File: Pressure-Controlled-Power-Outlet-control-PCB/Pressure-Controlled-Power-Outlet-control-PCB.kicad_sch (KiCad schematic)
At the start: 25 parts, among them J1 Analog water pressure sensor 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, J2 1017514, K1 PR27-24V-S-900-1A-EF, K2 PR27-24V-S-900-1A-EF, Q1 2N3906, Q2 IRF540N, Q3 IRF540N, Q4 2N3906, U1 Pico, U2 LM324, U3 LF50_TO220

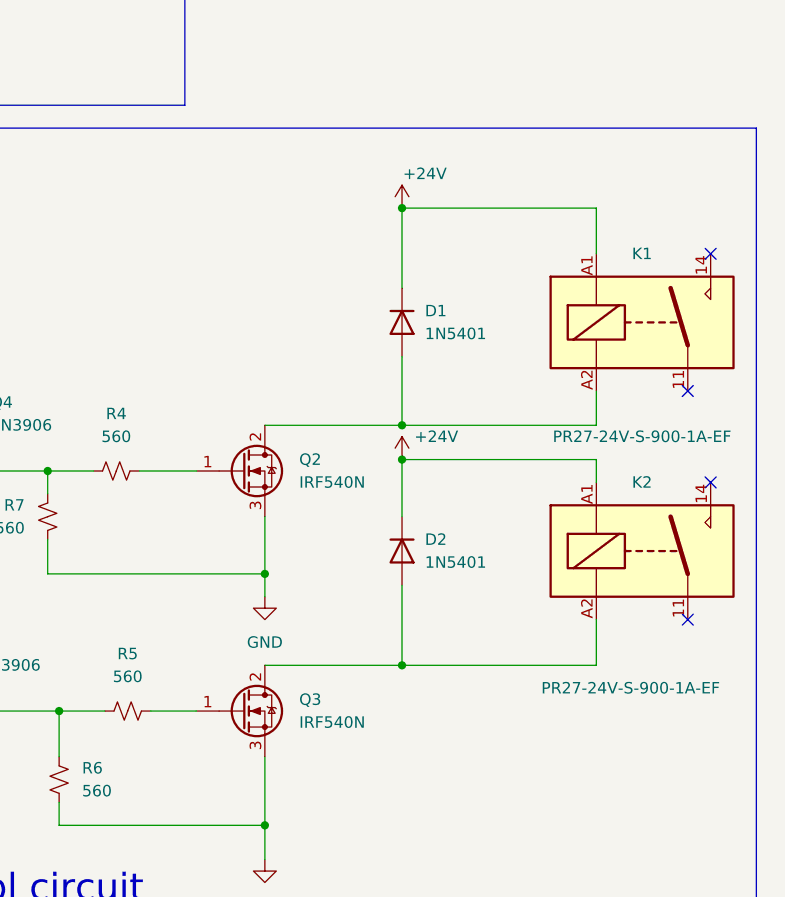
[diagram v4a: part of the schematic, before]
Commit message: added new relays
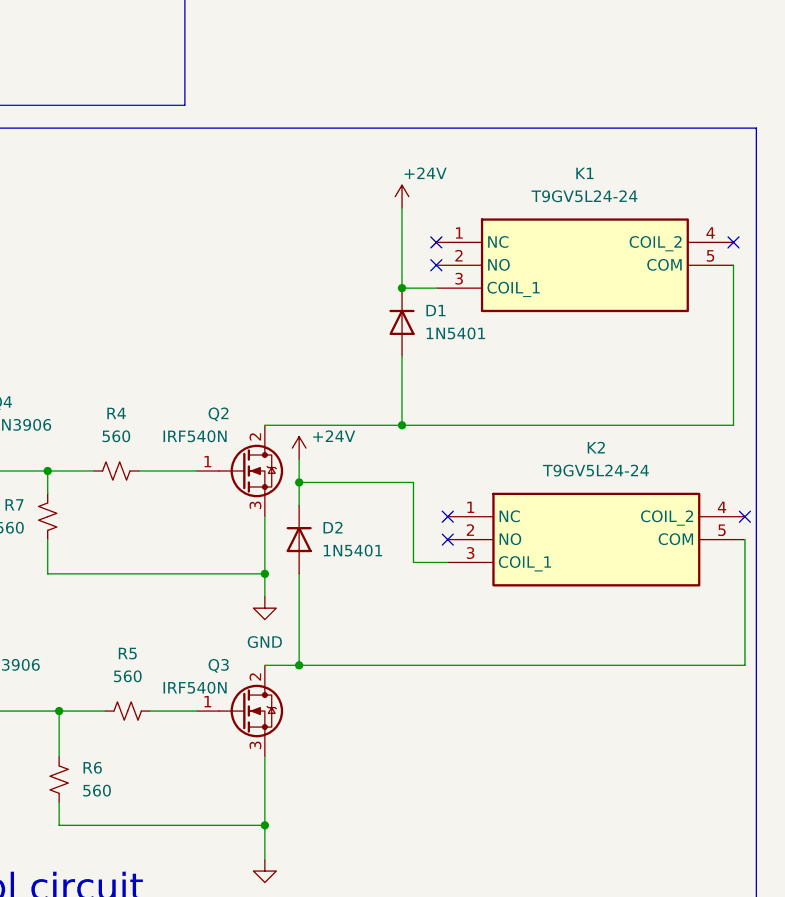
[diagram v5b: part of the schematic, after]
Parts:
- removed K1, K2: PR27-24V-S-900-1A-EF, Relay_THT:Relay_1-Form-A_Schrack-RYII_RM5mm, symbol Relay:Relay_SPST-NO
- added K1, K2: T9GV5L24-24, Extra:T9GV5L2424, symbol Extra:T9GV5L24-24
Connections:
- net +24V: now also K1.3 (COIL_1), K2.3 (COIL_1)
- net at D2.2 (A), Q3.2 (D): now also K2.5 (COM)
- net at D1.2 (A), Q2.2 (D): now also K1.5 (COM)
- no-connect marks 33 -> 35
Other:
- moved on the sheet: D2

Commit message: fixed PCB
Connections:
- net at D2.2 (A), Q3.2 (D): now also K2.4 (COIL_2); no longer K2.5 (COM)
- net at D1.2 (A), Q2.2 (D): now also K1.4 (COIL_2); no longer K1.5 (COM)
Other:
- moved on the sheet: K2
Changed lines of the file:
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@@
   )
   (no_connect (at 68.58 101.6))
-  (no_connect (at 245.11 106.68))
+  (no_connect (at 242.57 106.68))
   (no_connect (at 53.34 134.62))
   (no_connect (at 48.26 134.62))
@@
   (no_connect (at 68.58 83.82))
   (no_connect (at 33.02 104.14))
+  (no_connect (at 275.59 106.68))
   (no_connect (at 68.58 109.22))
-  (no_connect (at 278.13 104.14))
   (no_connect (at 33.02 88.9))
   (no_connect (at 33.02 116.84))
@@
   (no_connect (at 33.02 129.54))
   (no_connect (at 33.02 106.68))
+  (no_connect (at 276.86 76.2))
   (no_connect (at 68.58 91.44))
   (no_connect (at 33.02 127))
-  (no_connect (at 276.86 73.66))
   (no_connect (at 33.02 121.92))
   (no_connect (at 68.58 119.38))
   (no_connect (at 68.58 116.84))
   (no_connect (at 68.58 106.68))
-  (no_connect (at 245.11 104.14))
+  (no_connect (at 242.57 104.14))
   (no_connect (at 68.58 121.92))
   (no_connect (at 68.58 96.52))
@@
     (stroke (width 0) (type default))
   )
+  (wire (pts (xy 278.13 73.66) (xy 276.86 73.66))
+    (stroke (width 0) (type default))
+  )
   (wire (pts (xy 191.77 99.06) (xy 200.66 99.06))
     (stroke (width 0) (type default))
   )
-  (wire (pts (xy 278.13 106.68) (xy 278.13 120.65))
-    (stroke (width 0) (type default))
-  )
   (wire (pts (xy 162.56 40.64) (xy 162.56 43.18))
     (stroke (width 0) (type default))
   )
-  (wire (pts (xy 245.11 109.22) (xy 241.3 109.22))
+  (wire (pts (xy 242.57 109.22) (xy 241.3 109.22))
     (stroke (width 0) (type default))
   )
@@
     (stroke (width 0) (type default))
   )
+  (wire (pts (xy 278.13 120.65) (xy 278.13 104.14))
+    (stroke (width 0) (type default))
+  )
   (wire (pts (xy 241.3 109.22) (xy 241.3 100.33))
     (stroke (width 0) (type default))
@@
     (stroke (width 0) (type default))
   )
-  (wire (pts (xy 278.13 120.65) (xy 228.6 120.65))
+  (wire (pts (xy 228.6 120.65) (xy 278.13 120.65))
     (stroke (width 0) (type default))
   )
@@
     (stroke (width 0) (type default))
   )
+  (wire (pts (xy 240.03 93.98) (xy 278.13 93.98))
+    (stroke (width 0) (type default))
+  )
   (wire (pts (xy 175.26 119.38) (xy 182.88 119.38))
     (stroke (width 0) (type default))
@@
     (stroke (width 0) (type default))
   )
+  (wire (pts (xy 278.13 104.14) (xy 275.59 104.14))
+    (stroke (width 0) (type default))
+  )
   (wire (pts (xy 210.82 99.06) (xy 217.17 99.06))
     (stroke (width 0) (type default))
   )
+  (wire (pts (xy 278.13 93.98) (xy 278.13 73.66))
+    (stroke (width 0) (type default))
+  )
   (wire (pts (xy 212.09 125.73) (xy 217.17 125.73))
     (stroke (width 0) (type default))
@@
     (stroke (width 0) (type default))
   )
-  (wire (pts (xy 276.86 76.2) (xy 276.86 93.98))
-    (stroke (width 0) (type default))
-  )
   (wire (pts (xy 76.2 115.57) (xy 76.2 111.76))
     (stroke (width 0) (type default))
@@
   )
   (wire (pts (xy 114.3 168.91) (xy 111.76 168.91))
-    (stroke (width 0) (type default))
-  )
-  (wire (pts (xy 276.86 93.98) (xy 240.03 93.98))
     (stroke (width 0) (type default))
   )
@@
     )
   )
-  (symbol (lib_id "Extra:T9GV5L24-24") (at 245.11 104.14 0) (unit 1)
-    (in_bom yes) (on_board yes) (dnp no) (fields_autoplaced)
-    (property "Reference" "K2" (at 261.62 96.52 0)
-      (effects (font (size 1.27 1.27)))
-    )
-    (property "Value" "T9GV5L24-24" (at 261.62 99.06 0)
-      (effects (font (size 1.27 1.27)))
-    )
-    (property "Footprint" "Extra:T9GV5L2424" (at 274.32 199.06 0)
-      (effects (font (size 1.27 1.27)) (justify left top) hide)
-    )
-    (property "Datasheet" "https://www.te.com/commerce/DocumentDelivery/DDEController?Action=srchrtrv&DocNm=T9G&DocType=Data%20Sheet&DocLang=English&PartCntxt=1558670-7&DocFormat=pdf" (at 274.32 299.06 0)
-      (effects (font (size 1.27 1.27)) (justify left top) hide)
-    )
-    (property "Height" "27" (at 274.32 499.06 0)
-      (effects (font (size 1.27 1.27)) (justify left top) hide)
-    )
-    (property "Mouser Part Number" "655-T9GV5L24-24" (at 274.32 599.06 0)
-      (effects (font (size 1.27 1.27)) (justify left top) hide)
-    )
-    (property "Mouser Price/Stock" "https://www.mouser.co.uk/ProductDetail/TE-Connectivity-PB/T9GV5L24-24?qs=f9yNj16SXrJ%2FH2bWvrJZwA%3D%3D" (at 274.32 699.06 0)
-      (effects (font (size 1.27 1.27)) (justify left top) hide)
-    )
-    (property "Manufacturer_Name" "TE Connectivity" (at 274.32 799.06 0)
-      (effects (font (size 1.27 1.27)) (justify left top) hide)
-    )
-    (property "Manufacturer_Part_Number" "T9GV5L24-24" (at 274.32 899.06 0)
-      (effects (font (size 1.27 1.27)) (justify left top) hide)
-    )
+  (symbol (lib_id "Extra:T9GV5L24-24") (at 242.57 104.14 0) (unit 1)
+    (in_bom yes) (on_board yes) (dnp no) (fields_autoplaced)
+    (property "Reference" "K2" (at 259.08 96.52 0)
+      (effects (font (size 1.27 1.27)))
+    )
+    (property "Value" "T9GV5L24-24" (at 259.08 99.06 0)
+      (effects (font (size 1.27 1.27)))
+    )
+    (property "Footprint" "Extra:T9GV5L2424" (at 271.78 199.06 0)
+      (effects (font (size 1.27 1.27)) (justify left top) hide)
+    )
+    (property "Datasheet" "https://www.te.com/commerce/DocumentDelivery/DDEController?Action=srchrtrv&DocNm=T9G&DocType=Data%20Sheet&DocLang=English&PartCntxt=1558670-7&DocFormat=pdf" (at 271.78 299.06 0)
+      (effects (font (size 1.27 1.27)) (justify left top) hide)
+    )
+    (property "Height" "27" (at 271.78 499.06 0)
+      (effects (font (size 1.27 1.27)) (justify left top) hide)
+    )
+    (property "Mouser Part Number" "655-T9GV5L24-24" (at 271.78 599.06 0)
+      (effects (font (size 1.27 1.27)) (justify left top) hide)
+    )
+    (property "Mouser Price/Stock" "https://www.mouser.co.uk/ProductDetail/TE-Connectivity-PB/T9GV5L24-24?qs=f9yNj16SXrJ%2FH2bWvrJZwA%3D%3D" (at 271.78 699.06 0)
+      (effects (font (size 1.27 1.27)) (justify left top) hide)
+    )
+    (property "Manufacturer_Name" "TE Connectivity" (at 271.78 799.06 0)
+      (effects (font (size 1.27 1.27)) (justify left top) hide)
+    )
+    (property "Manufacturer_Part_Number" "T9GV5L24-24" (at 271.78 899.06 0)
+      (effects (font (size 1.27 1.27)) (justify left top) hide)
+    )

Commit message: should be done need to review the board to ensure everything is good
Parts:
- added unit 5 of U2
- R4, R5, R6, R7: value 560 -> 560 Ohm
- R8, R9: value 10K -> 10KOhm
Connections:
- net +5V: now also U2.4 (V+)
- net GND: now also U2.11 (V-)
- net ADC_Ref: no longer names the net of U1.35 (ADC_VREF)
- no-connect marks 35 -> 36
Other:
- title: (none) -> Pressure Controlled Power Outlet
- moved on the sheet: R3
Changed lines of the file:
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@@
 (kicad_sch (version 20230121) (generator eeschema)
   (paper "A4")
+  (title_block
+    (title "Pressure Controlled Power Outlet")
+    (date "2024-07-18")
+    (rev "V1.0")
+  )
   (junction (at 121.92 175.26) (diameter 0) (color 0 0 0 0)
   )
@@
   (no_connect (at 275.59 106.68))
   (no_connect (at 68.58 109.22))
+  (no_connect (at 68.58 93.98))
   (no_connect (at 33.02 88.9))
   (no_connect (at 33.02 116.84))
@@
     (stroke (width 0) (type default))
   )
-  (wire (pts (xy 77.47 99.06) (xy 91.44 99.06))
+  (wire (pts (xy 80.01 99.06) (xy 91.44 99.06))
     (stroke (width 0) (type default))
   )
@@
     (stroke (width 0) (type default))
   )
-  (wire (pts (xy 76.2 93.98) (xy 68.58 93.98))
-    (stroke (width 0) (type default))
-  )
   (wire (pts (xy 228.6 120.65) (xy 278.13 120.65))
     (stroke (width 0) (type default))
@@
     (stroke (width 0) (type default))
   )
-  (wire (pts (xy 68.58 99.06) (xy 72.39 99.06))
+  (wire (pts (xy 68.58 99.06) (xy 74.93 99.06))
     (stroke (width 0) (type default))
   )
@@
     (effects (font (size 1.27 1.27)) (justify right bottom))
   )
-  (label "ADC_Ref" (at 76.2 93.98 0) (fields_autoplaced)
-    (effects (font (size 1.27 1.27)) (justify left bottom))
-  )
   (label "Activate_Neutral" (at 166.37 119.38 180) (fields_autoplaced)
     (effects (font (size 1.27 1.27)) (justify right bottom))
@@
       (effects (font (size 1.27 1.27)))
     )
-    (property "Value" "10K" (at 172.72 88.9 90)
+    (property "Value" "10KOhm" (at 172.72 88.9 90)
       (effects (font (size 1.27 1.27)))
     )
@@
         (path "/db34d92e-5e84-4492-8b7e-15d9a09f9218"
           (reference "R8") (unit 1)
+        )
+      )
+    )
+  )
+  (symbol (lib_id "power:+5V") (at 162.56 158.75 0) (unit 1)
+    (in_bom yes) (on_board yes) (dnp no)
+    (property "Reference" "#PWR025" (at 162.56 162.56 0)
+      (effects (font (size 1.27 1.27)) hide)
+    )
+    (property "Value" "+5V" (at 165.1 157.48 0)
+      (effects (font (size 1.27 1.27)))
+    )
+    (property "Footprint" "" (at 162.56 158.75 0)
+      (effects (font (size 1.27 1.27)) hide)
+    )
+    (property "Datasheet" "" (at 162.56 158.75 0)
+      (effects (font (size 1.27 1.27)) hide)
+    )
+    (pin "1")
+    (instances
+      (project "Pressure-Controlled-Power-Outlet-control-PCB"
+        (path "/db34d92e-5e84-4492-8b7e-15d9a09f9218"
+          (reference "#PWR025") (unit 1)
         )
       )
@@
         (path "/db34d92e-5e84-4492-8b7e-15d9a09f9218"
           (reference "#PWR06") (unit 1)
+        )
+      )
+    )
+  )
+  (symbol (lib_id "Amplifier_Operational:LM324") (at 165.1 166.37 0) (unit 5)
+    (in_bom yes) (on_board yes) (dnp no) (fields_autoplaced)
+    (property "Reference" "U2" (at 163.83 165.1 0)
+      (effects (font (size 1.27 1.27)) (justify left))
+    )
+    (property "Value" "LM324" (at 163.83 167.64 0)
+      (effects (font (size 1.27 1.27)) (justify left))
+    )
+    (property "Footprint" "" (at 163.83 163.83 0)
+      (effects (font (size 1.27 1.27)) hide)
+    )
+    (property "Datasheet" "http://www.ti.com/lit/ds/symlink/lm2902-n.pdf" (at 166.37 161.29 0)
+      (effects (font (size 1.27 1.27)) hide)
+    )
+    (pin "7")
+    (pin "14")
+    (pin "9")
+    (pin "11")
+    (pin "3")
+    (pin "2")
+    (pin "8")
+    (pin "4")
+    (pin "10")
+    (pin "13")
+    (pin "12")
+    (pin "5")
+    (pin "6")
+    (pin "1")
+    (instances
+      (project "Pressure-Controlled-Power-Outlet-control-PCB"
+        (path "/db34d92e-5e84-4492-8b7e-15d9a09f9218"
+          (reference "U2") (unit 5)
         )
       )
@@
       (effects (font (size 1.27 1.27)))
     )
-    (property "Value" "560" (at 208.28 95.25 90)
+    (property "Value" "560 Ohm" (at 208.28 95.25 90)
       (effects (font (size 1.27 1.27)))
     )
@@
     )
   )
-  (symbol (lib_id "Device:R_Small_US") (at 74.93 99.06 90) (unit 1)
+  (symbol (lib_id "Device:R_Small_US") (at 77.47 99.06 90) (unit 1)
     (in_bom yes) (on_board yes) (dnp no)
-    (property "Reference" "R3" (at 74.93 96.52 90)
-      (effects (font (size 1.27 1.27)))
-    )
-    (property "Value" "0 Ohm" (at 74.93 101.6 90)
-      (effects (font (size 1.27 1.27)))
-    )
-    (property "Footprint" "Resistor_THT:R_Axial_DIN0207_L6.3mm_D2.5mm_P2.54mm_Vertical" (at 74.93 99.06 0)
-      (effects (font (size 1.27 1.27)) hide)
-    )
-    (property "Datasheet" "~" (at 74.93 99.06 0)
+    (property "Reference" "R3" (at 77.47 96.52 90)
+      (effects (font (size 1.27 1.27)))
+    )
+    (property "Value" "0 Ohm" (at 77.47 101.6 90)
+      (effects (font (size 1.27 1.27)))
+    )
+    (property "Footprint" "Resistor_THT:R_Axial_DIN0207_L6.3mm_D2.5mm_P2.54mm_Vertical" (at 77.47 99.06 0)
+      (effects (font (size 1.27 1.27)) hide)
+    )
+    (property "Datasheet" "~" (at 77.47 99.06 0)
       (effects (font (size 1.27 1.27)) hide)
     )
@@
         (path "/db34d92e-5e84-4492-8b7e-15d9a09f9218"
           (reference "R3") (unit 1)
+        )
+      )
+    )
+  )
+  (symbol (lib_id "power:GND") (at 162.56 173.99 0) (unit 1)
+    (in_bom yes) (on_board yes) (dnp no)
+    (property "Reference" "#PWR026" (at 162.56 180.34 0)
+      (effects (font (size 1.27 1.27)) hide)
+    )
+    (property "Value" "GND" (at 166.37 173.99 0)
+      (effects (font (size 1.27 1.27)))
+    )
+    (property "Footprint" "" (at 162.56 173.99 0)
+      (effects (font (size 1.27 1.27)) hide)
+    )
+    (property "Datasheet" "" (at 162.56 173.99 0)
+      (effects (font (size 1.27 1.27)) hide)
+    )
+    (pin "1")
+    (instances
+      (project "Pressure-Controlled-Power-Outlet-control-PCB"
+        (path "/db34d92e-5e84-4492-8b7e-15d9a09f9218"
+          (reference "#PWR026") (unit 1)
         )
       )
@@
       (effects (font (size 1.27 1.27)) (justify right))
     )
-    (property "Value" "560" (at 204.47 134.62 0)
+    (property "Value" "560 Ohm" (at 204.47 134.62 0)
       (effects (font (size 1.27 1.27)) (justify right))
     )
@@
       (effects (font (size 1.27 1.27)))
     )
-    (property "Value" "560" (at 209.55 121.92 90)
+    (property "Value" "560 Ohm" (at 209.55 121.92 90)
       (effects (font (size 1.27 1.27)))
     )
@@
   (symbol (lib_id "Device:R_Small_US") (at 200.66 104.14 0) (mirror x) (unit 1)
     (in_bom yes) (on_board yes) (dnp no)
-    (property "Reference" "R7" (at 198.12 102.87 0)
+    (property "Reference" "R7" (at 204.47 102.87 0)
       (effects (font (size 1.27 1.27)) (justify right))
     )
-    (property "Value" "560" (at 198.12 105.41 0)
+    (property "Value" "560 Ohm" (at 210.82 106.68 0)
       (effects (font (size 1.27 1.27)) (justify right))
     )
@@
       (effects (font (size 1.27 1.27)))
     )
-    (property "Value" "10K" (at 172.72 115.57 90)
-      (effects (font (size 1.27 1.27)))
-    )
+    (property "Value" "10KOhm" (at 172.72 115.57 90)
+      (effects (font (size 1.27 1.27)))
+    )
